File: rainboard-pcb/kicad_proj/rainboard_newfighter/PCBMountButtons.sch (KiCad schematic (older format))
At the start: 71 parts

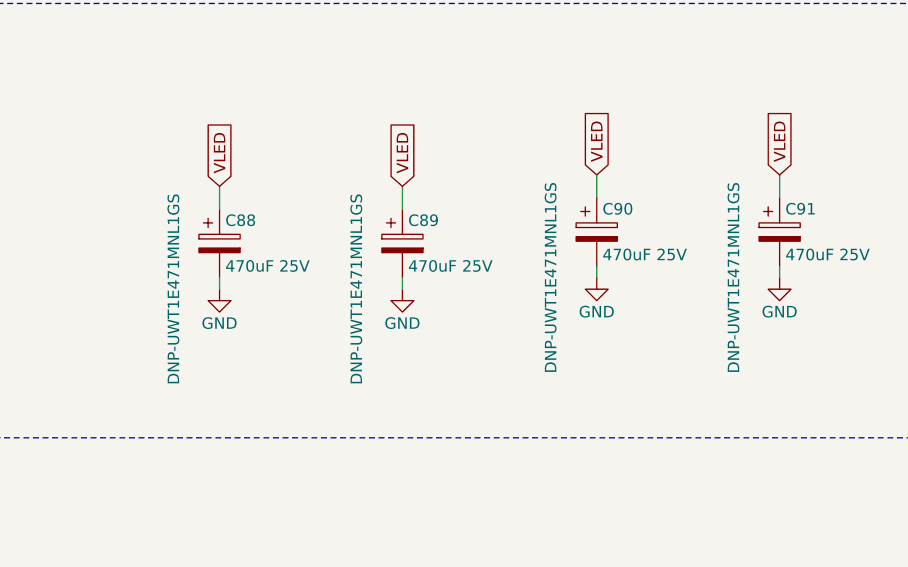
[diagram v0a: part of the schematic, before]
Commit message: Removed RGB from buttons, part numbers updated, cleaned up schematic
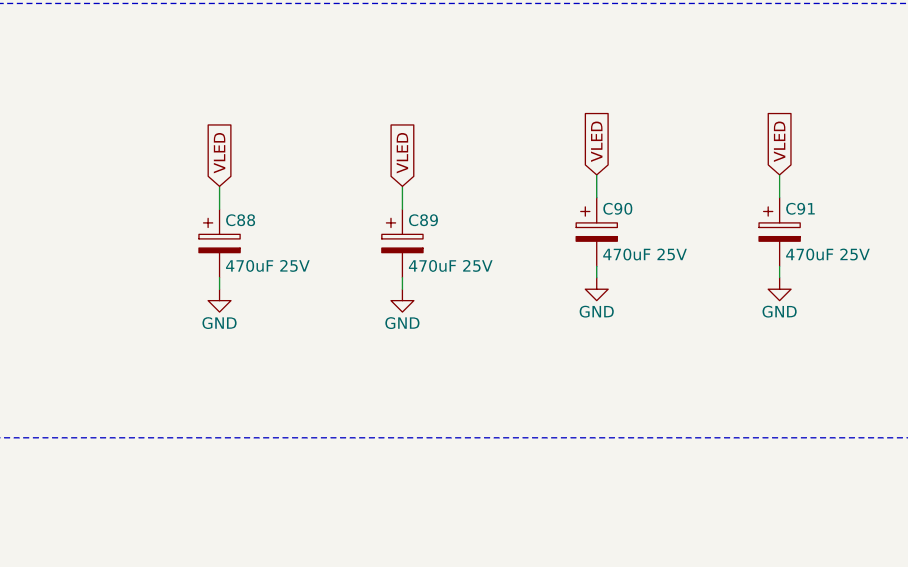
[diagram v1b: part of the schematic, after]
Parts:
- C88, C89, C90, C91: PN DNP-UWT1E471MNL1GS -> UCW1E471MNL1GS
- R100, R101, R102, R103, R104, R105, R106, R107, R108, R109, R110, R111, R112, R113, R114, R115, R116, R117, R118, R119, R120, R121, R122, R123, R124, R125, R126, R127, R128, R129, R130, R74, R75, R76, R77, R78, R79, R80, R81, R82, R83, R84, R85, R86, R87, R88, R89, R90, R91, R92, R93, R94, R95, R96, R97, R98, R99: PN (none) -> RC0603FR-07210RL

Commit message: Moves meta buttons to correct config, adds back on board buttons.
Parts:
- removed R114: 210R, Resistor_SMD:R_0805_2012Metric, symbol Device:R
- added R104, R109, R94, R99: 210R, Resistor_SMD:R_0805_2012Metric, symbol Device:R
- renumbered C88 to C51, C89 to C52, C90 to C53, C91 to C54, C92 to C55, C93 to C56, C94 to C57, C95 to C58, C96 to C59, C97 to C60, C98 to C61, C99 to C62, C100 to C63, C101 to C64, R119 to R100, R120 to R101, R121 to R102, R122 to R103, R123 to R105, R124 to R106, R125 to R107, R126 to R108, R127 to R110, R128 to R111, R129 to R112, R130 to R113, R74 to R54, R75 to R55, R76 to R56, R77 to R57, R78 to R58, R79 to R59, R80 to R60, R81 to R61, R82 to R62, R83 to R63, R84 to R64, R85 to R65, R86 to R66, R87 to R67, R88 to R68, R89 to R69, R90 to R70, R91 to R71, R92 to R72, R93 to R73, R94 to R74, R95 to R75, R96 to R76, R97 to R77, R98 to R78, R99 to R79, R100 to R80, R101 to R81, R102 to R82, R103 to R83, R104 to R84, R105 to R85, R106 to R86, R107 to R87, R108 to R88, R109 to R89, R110 to R90, R111 to R91, R112 to R92, R113 to R93, R115 to R95, R116 to R96, R117 to R97, R118 to R98
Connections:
- net sheet6001C1E9/DOUT: now also R94.1
- new net sheet6112CF44/DIN: R94.2
- new net sheet6112CF44/DOUT: R99.1
- new net sheet61155765/DIN: R99.2
- new net sheet61155765/DOUT: R104.1
- new net sheet611F5592/DIN: R104.2
- new net sheet611F5592/DOUT: R109.1
- new net sheet6120995A/DIN: R109.2
- no-connect marks 0 -> 1

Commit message: Modified electrolytics and setup board for layout
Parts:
- C51, C52, C53, C54: value 470uF 25V -> 470uF 10V; footprint Capacitor_SMD:CP_Elec_10x10 -> Capacitor_SMD:CP_Elec_6.3x7.7
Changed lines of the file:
@@
 AR Path="/6000B457/6031D4FF" Ref="C?"  Part="1"
 F 0 "C54" H 11075 2300 50  0000 L CNN
-F 1 "470uF 25V" H 11075 2100 50  0000 L CNN
-F 2 "Capacitor_SMD:CP_Elec_10x10" H 11088 2050 50  0001 C CNN
+F 1 "470uF 10V" H 11075 2100 50  0000 L CNN
+F 2 "Capacitor_SMD:CP_Elec_6.3x7.7" H 11088 2050 50  0001 C CNN
 F 3 "~" H 11050 2200 50  0001 C CNN
 F 4 "UCW1E471MNL1GS" V 10850 2000 50  0001 C CNN "PN"
@@
 AR Path="/6000B457/6031F351" Ref="C?"  Part="1"
 F 0 "C53" H 10275 2300 50  0000 L CNN
-F 1 "470uF 25V" H 10275 2100 50  0000 L CNN
-F 2 "Capacitor_SMD:CP_Elec_10x10" H 10288 2050 50  0001 C CNN
+F 1 "470uF 10V" H 10275 2100 50  0000 L CNN
+F 2 "Capacitor_SMD:CP_Elec_6.3x7.7" H 10288 2050 50  0001 C CNN
 F 3 "~" H 10250 2200 50  0001 C CNN
 F 4 "UCW1E471MNL1GS" V 10050 2000 50  0001 C CNN "PN"
@@
 AR Path="/6000B457/60320379" Ref="C?"  Part="1"
 F 0 "C52" H 9425 2350 50  0000 L CNN
-F 1 "470uF 25V" H 9425 2150 50  0000 L CNN
-F 2 "Capacitor_SMD:CP_Elec_10x10" H 9438 2100 50  0001 C CNN
+F 1 "470uF 10V" H 9425 2150 50  0000 L CNN
+F 2 "Capacitor_SMD:CP_Elec_6.3x7.7" H 9438 2100 50  0001 C CNN
 F 3 "~" H 9400 2250 50  0001 C CNN
 F 4 "UCW1E471MNL1GS" V 9200 2050 50  0001 C CNN "PN"
@@
 AR Path="/6000B457/60320391" Ref="C?"  Part="1"
 F 0 "C51" H 8625 2350 50  0000 L CNN
-F 1 "470uF 25V" H 8625 2150 50  0000 L CNN
-F 2 "Capacitor_SMD:CP_Elec_10x10" H 8638 2100 50  0001 C CNN
+F 1 "470uF 10V" H 8625 2150 50  0000 L CNN
+F 2 "Capacitor_SMD:CP_Elec_6.3x7.7" H 8638 2100 50  0001 C CNN
 F 3 "~" H 8600 2250 50  0001 C CNN
 F 4 "UCW1E471MNL1GS" V 8400 2050 50  0001 C CNN "PN"

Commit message: Forgot to update electrolytic PN
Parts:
- C51, C52, C53, C54: PN UCW1E471MNL1GS -> EEE-FTA471XAP
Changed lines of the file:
@@
 F 2 "Capacitor_SMD:CP_Elec_6.3x7.7" H 11088 2050 50  0001 C CNN
 F 3 "~" H 11050 2200 50  0001 C CNN
-F 4 "UCW1E471MNL1GS" V 10850 2000 50  0001 C CNN "PN"
+F 4 "EEE-FTA471XAP" V 10850 2000 50  0001 C CNN "PN"
 	1    11050 2200
 	1    0    0    -1
@@
 F 2 "Capacitor_SMD:CP_Elec_6.3x7.7" H 10288 2050 50  0001 C CNN
 F 3 "~" H 10250 2200 50  0001 C CNN
-F 4 "UCW1E471MNL1GS" V 10050 2000 50  0001 C CNN "PN"
+F 4 "EEE-FTA471XAP" V 10050 2000 50  0001 C CNN "PN"
 	1    10250 2200
 	1    0    0    -1
@@
 F 2 "Capacitor_SMD:CP_Elec_6.3x7.7" H 9438 2100 50  0001 C CNN
 F 3 "~" H 9400 2250 50  0001 C CNN
-F 4 "UCW1E471MNL1GS" V 9200 2050 50  0001 C CNN "PN"
+F 4 "EEE-FTA471XAP" V 9200 2050 50  0001 C CNN "PN"
 	1    9400 2250
 	1    0    0    -1
@@
 F 2 "Capacitor_SMD:CP_Elec_6.3x7.7" H 8638 2100 50  0001 C CNN
 F 3 "~" H 8600 2250 50  0001 C CNN
-F 4 "UCW1E471MNL1GS" V 8400 2050 50  0001 C CNN "PN"
+F 4 "EEE-FTA471XAP" V 8400 2050 50  0001 C CNN "PN"
 	1    8600 2250
 	1    0    0    -1
